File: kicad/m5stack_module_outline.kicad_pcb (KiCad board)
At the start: 2 copper layers, 50 x 50 mm, 13 parts, among them J1 Conn_02x15_Odd_Even

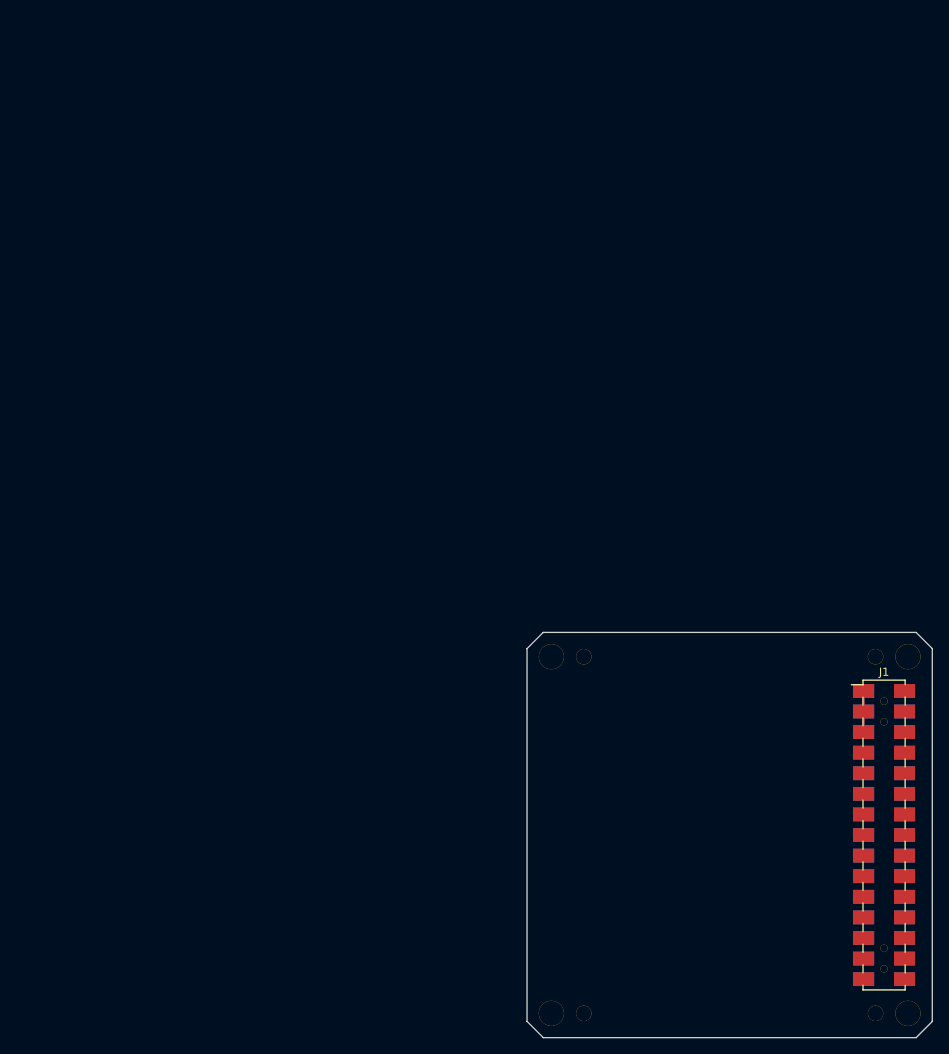
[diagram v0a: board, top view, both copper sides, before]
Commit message: Add m5stack pinheader, route, etc.
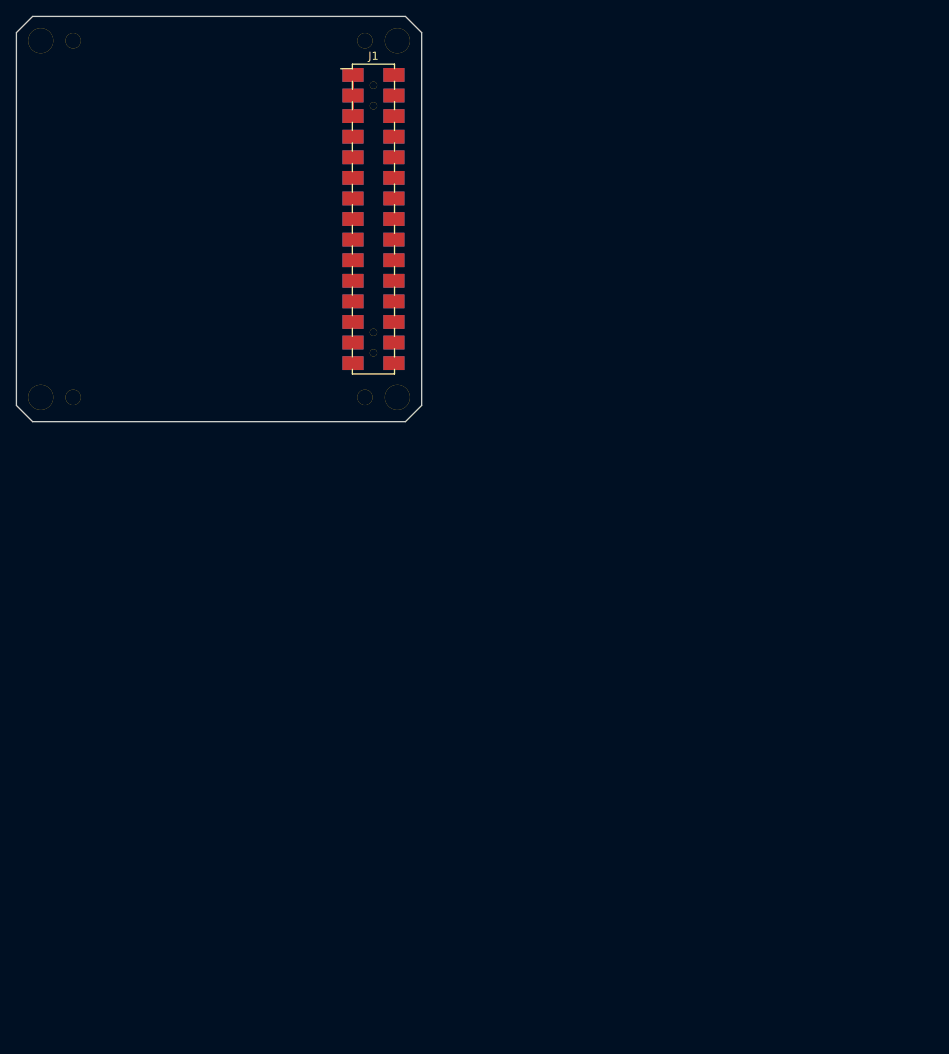
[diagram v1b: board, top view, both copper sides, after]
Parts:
- moved ? 98.7 mm to (-1.95, -17.5)
- moved ? 98.7 mm to (-43.0, -12.0)
- moved ? 98.7 mm to (-1.95, -48.0)
- moved ? 98.7 mm to (-1.95, -50.5)
- moved ? 98.7 mm to (-1.95, -20.0)
- moved ? 98.7 mm to (-43.0, -56.0)
- moved ? 98.7 mm to (-39.0, -56.0)
- moved ? 98.7 mm to (1.00, -56.0)
- moved ? 98.7 mm to (-3.00, -56.0)
- moved ? 98.7 mm to (1.00, -12.0)
- moved ? 98.7 mm to (-3.00, -12.0)
- moved ? 98.7 mm to (-39.0, -12.0)
- moved J1 98.7 mm to (-1.95, -34.0)
